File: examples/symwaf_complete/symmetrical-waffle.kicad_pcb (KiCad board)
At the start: 2 copper layers, 38 parts, among them J1 ICSP, J2 FTDI Programmer, J3 GPIO Header, SW1 SW_Push, SW2 SW_DIP_x01, U1 ATMEGA328-AU, U10 ws2812b, U11 ws2812b, U12 ws2812b, U13 ws2812b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

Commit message: Working on the "complete" board layout"
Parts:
- C5, C6, Y1: moved to B.Cu
- moved C5 79.5 mm to (132.0, 82.2)
- moved C6 79.1 mm to (141.0, 81.2), turned to 270 degrees
- moved C7 78.4 mm to (120.2, 63.0), turned to 270 degrees
- moved C18 75.1 mm to (118.2, 66.2)
- moved C17 71.3 mm to (114.2, 76.2)
- moved U1 69.9 mm to (134.0, 75.0), turned to 90 degrees
- moved C16 67.1 mm to (116.5, 86.2)
- moved C8 66.4 mm to (130.2, 60.5), turned to 270 degrees
- moved C9 57.8 mm to (140.0, 61.0), turned to 270 degrees
- moved C10 54.5 mm to (147.8, 67.2), turned to 270 degrees
- moved C14 50.1 mm to (135.2, 96.2)
- moved Y1 49.5 mm to (135.0, 82.2)
- moved C15 48.4 mm to (125.2, 93.8)
- moved C11 46.7 mm to (150.5, 80.0), turned to 270 degrees
- moved C12 40.3 mm to (148.0, 90.0), turned to 270 degrees
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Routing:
- net VCC: track 0.00 -> 121.1 mm, vias 0 -> 2
- net Net-(U2-Pad2): track 0.00 -> 18.8 mm
- net Net-(U12-Pad2): track 0.00 -> 18.7 mm
- net Net-(U3-Pad2): track 0.00 -> 16.6 mm
- net Net-(U6-Pad2): track 0.00 -> 16.5 mm
- net Net-(U4-Pad2): track 0.00 -> 15.5 mm
- net Net-(U11-Pad2): track 0.00 -> 15.3 mm
- net Net-(U5-Pad2): track 0.00 -> 14.8 mm
- net Net-(U10-Pad2): track 0.00 -> 13.5 mm
- net /LEDSignal: track 0.00 -> 12.0 mm
- net Net-(U10-Pad4): track 0.00 -> 9.32 mm
- net /XTAL2: track 0.00 -> 6.79 mm
- net /LED Ring/ROW_2: track 0.00 -> 5.45 mm
- net Net-(U8-Pad2): track 0.00 -> 5.43 mm
- net /XTAL1: track 0.00 -> 5.39 mm
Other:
- board outline added: 50 x 50 mm

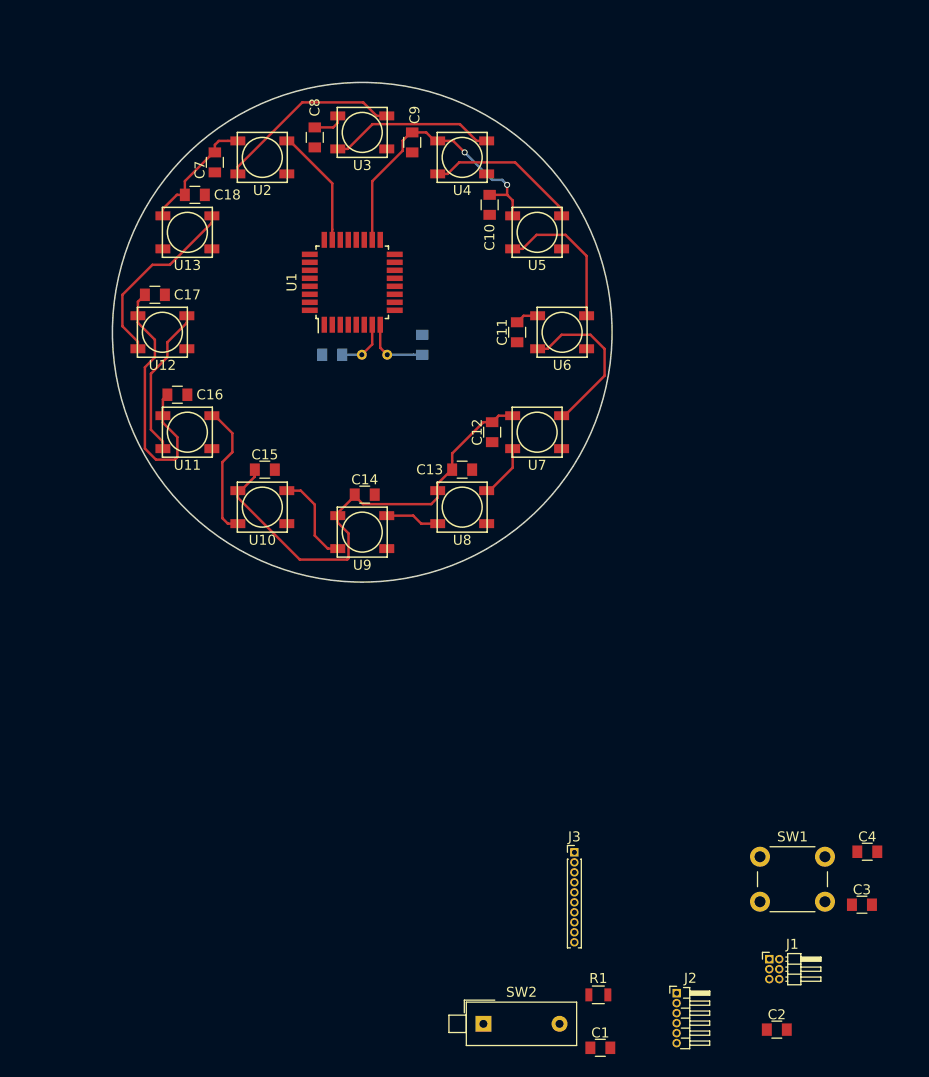
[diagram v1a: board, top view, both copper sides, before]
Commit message: We might want to switch out the switches to something more smaller
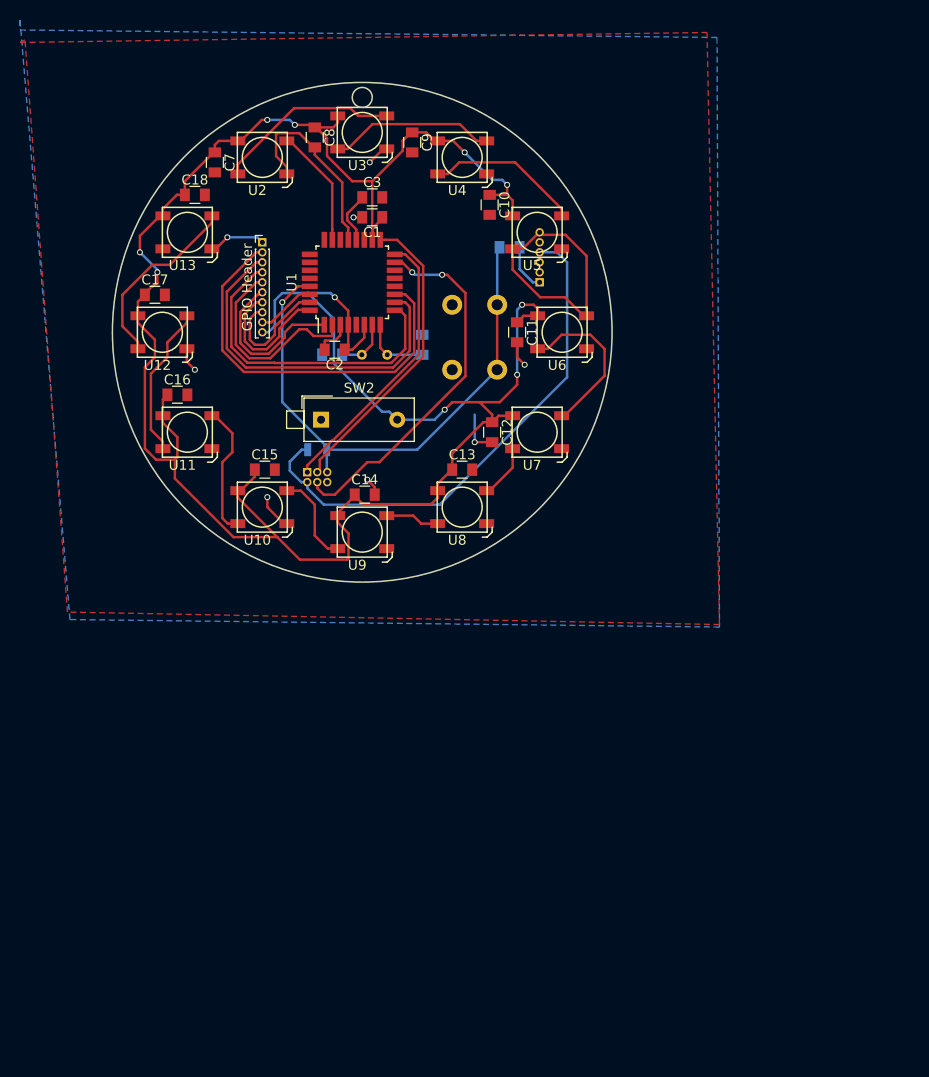
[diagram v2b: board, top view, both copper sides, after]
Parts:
- C4, J1, J2, R1, SW1: moved to B.Cu
- GPIO Header: renamed from J3
- moved C1 86.2 mm to (136.0, 68.5), turned to 180 degrees
- moved C3 86.1 mm to (136.0, 66.5)
- moved C2 81.2 mm to (132.2, 81.8), turned to 180 degrees
- moved J2 72.4 mm to (152.8, 75.0)
- moved C4 70.3 mm to (149.8, 71.5), turned to 180 degrees
- moved GPIO Header 68.6 mm to (125.0, 71.0)
- moved J1 67.2 mm to (129.5, 94.0), turned to 270 degrees
- moved SW2 62.6 mm to (130.9, 88.8)
- moved R1 61.4 mm to (130.5, 91.8)
- moved SW1 55.4 mm to (148.5, 83.8), turned to 90 degrees
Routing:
- net VCC: track 121.1 -> 230.3 mm, vias 2 -> 10
- net GND: track 0.00 -> 60.2 mm, vias 0 -> 8
- net /RST_CIRCUIT: track 0.00 -> 55.0 mm, vias 0 -> 1
- net +5V: track 0.00 -> 52.7 mm
- net /GPIO_7: track 0.00 -> 40.0 mm
- net /MOSI: track 0.00 -> 37.3 mm, vias 0 -> 2
- net /GPIO_6: track 0.00 -> 36.3 mm
- net /GPIO_5: track 0.00 -> 32.4 mm
- net /SCK: track 0.00 -> 30.4 mm
- net /MISO: track 0.00 -> 28.1 mm
- net /GPIO_4: track 0.00 -> 20.5 mm
- net /GPIO_3: track 0.00 -> 16.5 mm
- net /GPIO_2: track 0.00 -> 13.9 mm
- net /GPIO_1: track 0.00 -> 12.1 mm
- net /GPIO_0: track 0.00 -> 5.91 mm
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- added copper zone on B.Cu, net GND
- added copper zone on F.Cu, net GND
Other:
- outline, holes or cut-outs redrawn
- board text added: "Hang this on your Christmas Tree (Your parents will think you're weird)"

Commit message: Creating a simpler version of the example board
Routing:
- net GND: track 60.2 -> 65.7 mm, vias 8 -> 9
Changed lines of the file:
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@@
     (thickness 1.6)
     (drawings 3)
-    (tracks 407)
+    (tracks 413)
     (zones 0)
     (modules 38)
@@
     (last_trace_width 0.25)
     (trace_clearance 0.2)
-    (zone_clearance 0.508)
+    (zone_clearance 0.2)
     (zone_45_only no)
     (trace_min 0.2)
@@
       (effects (font (size 1 1) (thickness 0.15)) (justify mirror))
     )
-    (fp_text value "FTDI Programmer" (at 1.375 -6.5) (layer B.Fab)
+    (fp_text value "FTDI Programmer" (at -3.25 -7) (layer B.Fab)
       (effects (font (size 1 1) (thickness 0.15)) (justify mirror))
     )
@@
   (segment (start 132.1 59.5) (end 132.55 59.05) (width 0.25) (layer F.Cu) (net 1))
   (segment (start 132.55 59.05) (end 132.55 58.35) (width 0.25) (layer F.Cu) (net 1))
+  (segment (start 131.35 76.75) (end 131.35 75.4) (width 0.25) (layer F.Cu) (net 2))
+  (segment (start 131.35 75.4) (end 131.5 75.25) (width 0.25) (layer F.Cu) (net 2))
+  (segment (start 133.6 73.9) (end 132.25 75.25) (width 0.25) (layer F.Cu) (net 2))
+  (segment (start 131.25 81.75) (end 130 81.75) (width 0.25) (layer F.Cu) (net 2))
+  (segment (start 130 81.75) (end 129.5 81.25) (width 0.25) (layer F.Cu) (net 2))
+  (via (at 129.5 81.25) (size 0.6) (drill 0.4) (layers F.Cu B.Cu) (net 2))
   (segment (start 146.25 91) (end 146.25 88.25) (width 0.25) (layer B.Cu) (net 2))
   (segment (start 148 91) (end 146.25 91) (width 0.25) (layer F.Cu) (net 2))
@@
       )
     )
+  )
+  (zone (net 2) (net_name GND) (layer F.Cu) (hatch edge 0.508)
+    (connect_pads (clearance 0.2))
+    (min_thickness 0.254)
+    (fill yes (arc_segments 16) (thermal_gap 0.508) (thermal_bridge_width 0.508))
+    (polygon
+      (pts
+        (xy 129.75 70.75) (xy 138.5 70.75) (xy 138.5 79.75) (xy 129.75 79.75)
+      )
+    )
